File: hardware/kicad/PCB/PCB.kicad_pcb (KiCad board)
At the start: 2 copper layers, 19 parts, among them J1 USB_C_Receptacle_PowerOnly_6P, J2 Conn_01x05_Socket, J3 Conn_01x02, U1 STM32G030F6Px, U2 MCP73831-2-OT, U3 DW01A, U4 FS8205A_C2830320

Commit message: updated PCB design
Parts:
- added C4: 1uF, Capacitor_SMD:C_0603_1608Metric, F.Cu at (18.0, 23.8)
- added C5: 1uF, Capacitor_SMD:C_0603_1608Metric, F.Cu at (18.0, 26.3)
- added C6: 100nF, Capacitor_SMD:C_0603_1608Metric, F.Cu at (18.0, 28.8)
- added D10: LED, Diode_SMD:D_0603_1608Metric, F.Cu at (38.1, 18.9)
- added D11: LED, Diode_SMD:D_0603_1608Metric, F.Cu at (38.1, 21.5)
- added D12: LED, Diode_SMD:D_0603_1608Metric, F.Cu at (38.1, 24.1)
- added D13: LED, Diode_SMD:D_0603_1608Metric, F.Cu at (38.1, 26.7)
- added D14: LED, Diode_SMD:D_0603_1608Metric, F.Cu at (38.1, 29.2)
- added D15: LED, Diode_SMD:D_0603_1608Metric, F.Cu at (38.1, 31.8)
- added D16: LED, Diode_SMD:D_0603_1608Metric, F.Cu at (42.2, 16.3)
- added D17: LED, Diode_SMD:D_0603_1608Metric, F.Cu at (42.2, 18.9)
- added D18: LED, Diode_SMD:D_0603_1608Metric, F.Cu at (42.2, 21.5)
- added D19: LED, Diode_SMD:D_0603_1608Metric, F.Cu at (42.2, 24.1)
- added D20: LED, Diode_SMD:D_0603_1608Metric, F.Cu at (42.2, 26.7)
- added D21: LED, Diode_SMD:D_0603_1608Metric, F.Cu at (42.2, 29.2)
- added D22: LED, Diode_SMD:D_0603_1608Metric, F.Cu at (42.2, 31.8)
- added D3: D_Schottky, Sensor_Humidity:Sensirion_DFN-4_1.5x1.5mm_P0.8mm_SHT4x_NoCentralPad, F.Cu at (46.2, 31.4)
- added D4: LED, Diode_SMD:D_0603_1608Metric, F.Cu at (34.1, 21.5)
- added D5: LED, Diode_SMD:D_0603_1608Metric, F.Cu at (34.1, 24.1)
- added D6: LED, Diode_SMD:D_0603_1608Metric, F.Cu at (34.1, 26.7)
- added D7: LED, Diode_SMD:D_0603_1608Metric, F.Cu at (34.1, 29.2)
- added D8: LED, Diode_SMD:D_0603_1608Metric, F.Cu at (34.1, 31.8)
- added D9: LED, Diode_SMD:D_0603_1608Metric, F.Cu at (38.1, 16.3)
- added R10: 470, Resistor_SMD:R_0603_1608Metric, F.Cu at (22.0, 31.3)
- added R11: 470, Resistor_SMD:R_0603_1608Metric, F.Cu at (22.0, 33.8)
- added R12: 470, Resistor_SMD:R_0603_1608Metric, F.Cu at (22.0, 36.3)
- added R13: 470, Resistor_SMD:R_0603_1608Metric, F.Cu at (26.0, 16.3)
- added R14: 470, Resistor_SMD:R_0603_1608Metric, F.Cu at (26.0, 18.8)
- added R15: 470, Resistor_SMD:R_0603_1608Metric, F.Cu at (26.0, 21.3)
- added R16: 470, Resistor_SMD:R_0603_1608Metric, F.Cu at (26.0, 23.8)
- added R17: 470, Resistor_SMD:R_0603_1608Metric, F.Cu at (26.0, 26.3)
- added R18: 470, Resistor_SMD:R_0603_1608Metric, F.Cu at (26.0, 28.8)
- added R19: 470, Resistor_SMD:R_0603_1608Metric, F.Cu at (26.0, 31.3)
- added R20: 470, Resistor_SMD:R_0603_1608Metric, F.Cu at (26.0, 33.8)
- added R21: 470, Resistor_SMD:R_0603_1608Metric, F.Cu at (26.0, 36.3)
- added R22: 470, Resistor_SMD:R_0603_1608Metric, F.Cu at (30.0, 16.3)
- added R23: 470, Resistor_SMD:R_0603_1608Metric, F.Cu at (30.0, 18.8)
- added R24: 470, Resistor_SMD:R_0603_1608Metric, F.Cu at (30.0, 21.3)
- added R25: 470, Resistor_SMD:R_0603_1608Metric, F.Cu at (30.0, 23.8)
- added R26: 470, Resistor_SMD:R_0603_1608Metric, F.Cu at (30.0, 26.3)
- added R27: 1M, Resistor_SMD:R_0603_1608Metric, F.Cu at (30.0, 28.8)
- added R28: 1M, Resistor_SMD:R_0603_1608Metric, F.Cu at (30.0, 31.3)
- added R7: 470, Resistor_SMD:R_0603_1608Metric, F.Cu at (22.0, 23.8)
- added R8: 470, Resistor_SMD:R_0603_1608Metric, F.Cu at (22.0, 26.3)
- added R9: 470, Resistor_SMD:R_0603_1608Metric, F.Cu at (22.0, 28.8)
- added U5: TPS7A0233PDBVR, JLC2KiCad:SOT-23-5_L2.9-W1.6-P0.95-LS2.8-BR, F.Cu at (46.6, 27.6)
- moved U4 33.3 mm to (46.9, 22.9)
- moved R5 31.3 mm to (22.0, 18.8)
- moved R6 31.3 mm to (22.0, 21.3)
- moved R4 31.3 mm to (22.0, 16.3)
- moved D1 31.3 mm to (34.1, 16.3)
- moved D2 31.3 mm to (34.1, 18.9)
- moved KEY1 23.4 mm to (47.6, 17.7)
- moved C1 19.0 mm to (18.0, 16.3)
- moved C2 19.0 mm to (18.0, 18.8)
- moved C3 19.0 mm to (18.0, 21.3)
- moved J3 18.4 mm to (37.3, 46.7)
- moved J2 16.6 mm to (23.5, 40.0)
- moved R2 13.6 mm to (18.0, 33.8)
- moved R3 13.6 mm to (18.0, 36.3)
- moved R1 13.6 mm to (18.0, 31.3)
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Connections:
- D2 pad 1: unconnected-(D2-K-Pad1) -> TIM14_CH1
- D2 pad 2: unconnected-(D2-A-Pad2) -> Net-(D2-A)
- J2 pad 1: unconnected-(J2-Pin_1-Pad1) -> Net-(D3-A)
- U1 pad 1: unconnected-(U1-PB7/PB8-Pad1) -> TIM16_CH1
- U1 pad 11: unconnected-(U1-PA4-Pad11) -> TIM14_CH1
- U1 pad 13: unconnected-(U1-PA6-Pad13) -> TIM3_CH1
- U1 pad 14: unconnected-(U1-PA7-Pad14) -> TIM3_CH2
- U1 pad 15: unconnected-(U1-PA8/PB0/PB1/PB2-Pad15) -> TIM1_CH2N
- U1 pad 16: unconnected-(U1-PA9/PA11-Pad16) -> TIM1_CH4
- U1 pad 20: unconnected-(U1-PB3/PB4/PB5/PB6-Pad20) -> TIM1_CH3
- U1 pad 4: unconnected-(U1-VDD-Pad4) -> PROG_PWR
- U1 pad 8: unconnected-(U1-PA1-Pad8) -> PA1

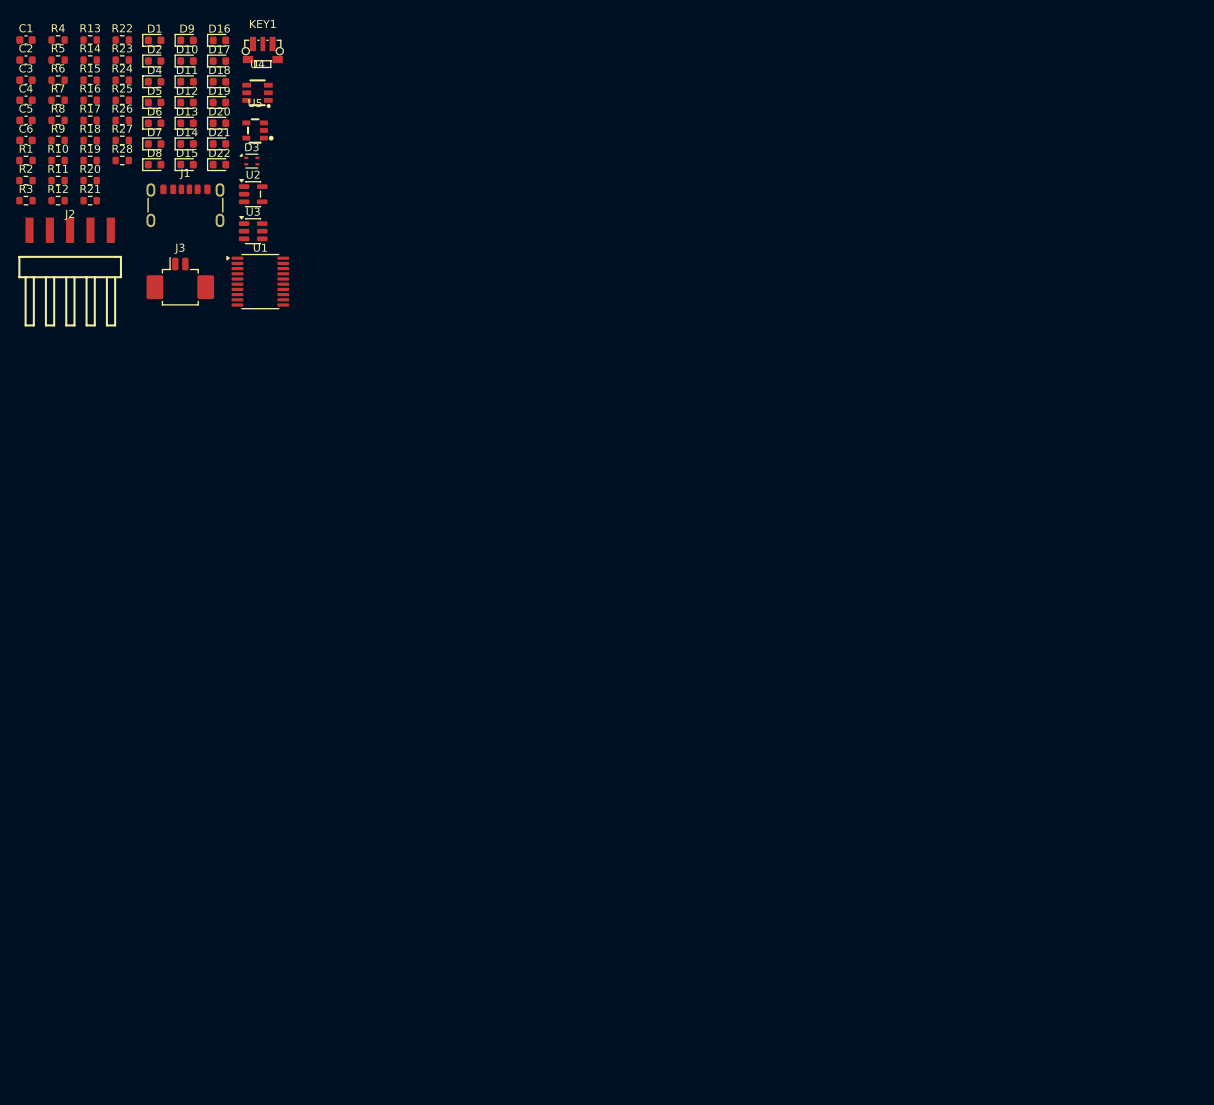
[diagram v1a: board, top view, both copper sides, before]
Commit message: Major update to PCB layout, nearly ready for first batch (#8)
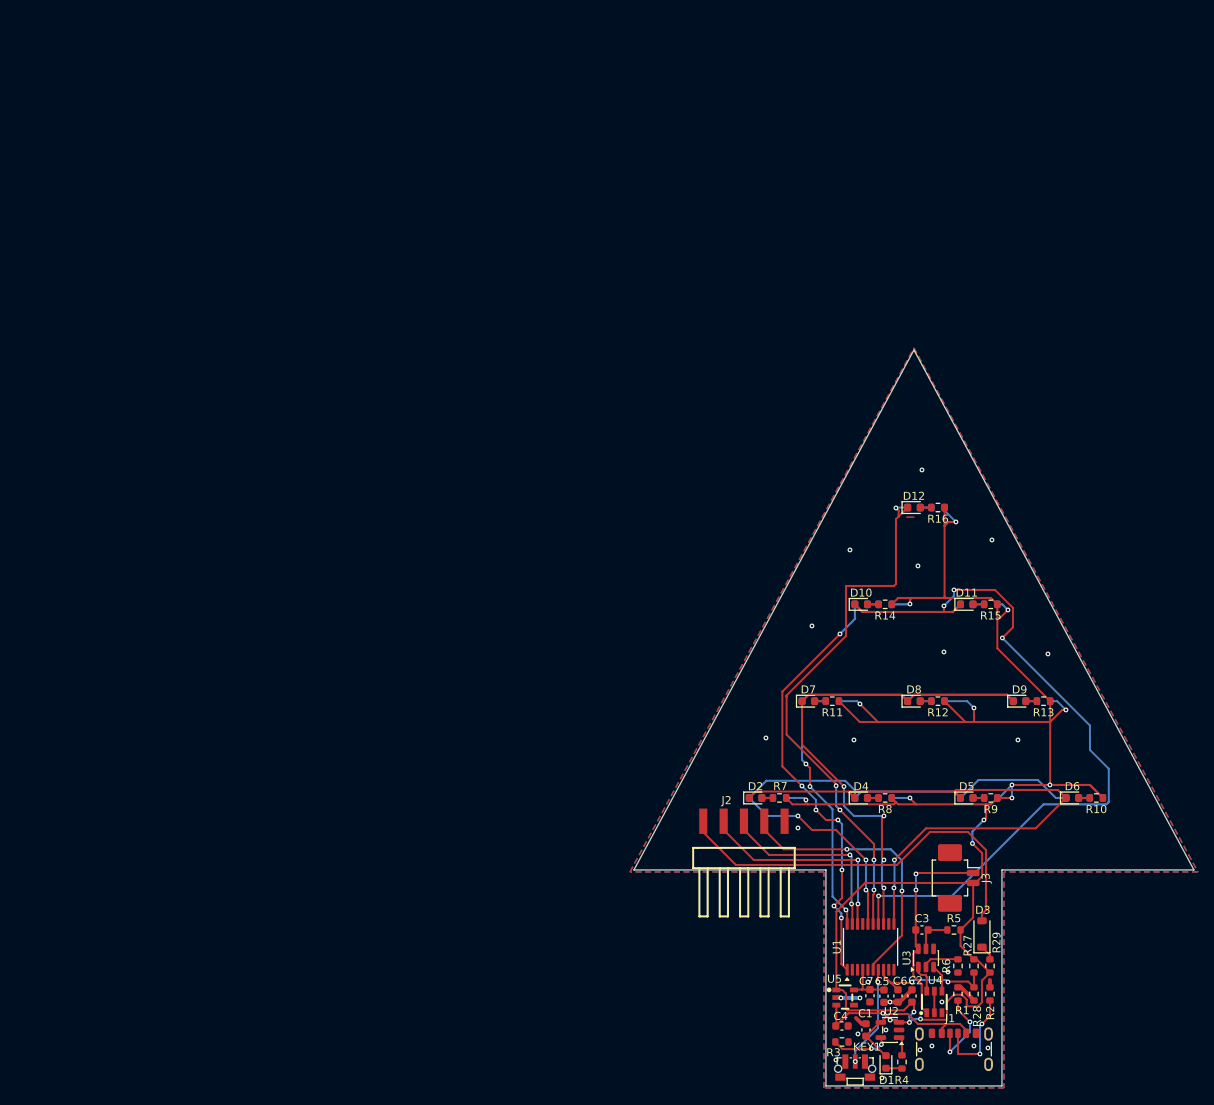
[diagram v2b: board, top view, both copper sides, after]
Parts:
- added C7: 100nF, Capacitor_SMD:C_0603_1608Metric, F.Cu at (123.5, 135.7)
- added R29: 33, Resistor_SMD:R_0603_1608Metric, F.Cu at (138.5, 132.0)
- D13, D14, D15, D16, D17, D18, D19, D20, D21, D22, R17, R18, R19, R20, R21, R22, R23, R24, R25, R26: moved to B.Cu
- D3: footprint Sensor_Humidity:Sensirion_DFN-4_1.5x1.5mm_P0.8mm_SHT4x_NoCentralPad -> Diode_SMD:D_SOD-123
- moved R4 165.7 mm to (127.5, 144.0), turned to 90 degrees
- moved C1 162.3 mm to (123.0, 140.0), turned to -90 degrees
- moved C2 161.1 mm to (128.8, 135.8), turned to 90 degrees
- moved R6 157.8 mm to (134.5, 132.0), turned to 90 degrees
- moved R2 157.7 mm to (138.5, 135.5), turned to 90 degrees
- moved D1 157.1 mm to (125.5, 144.0), turned to 90 degrees
- moved R1 156.3 mm to (134.5, 135.5), turned to 90 degrees
- moved R5 156.1 mm to (134.0, 127.5)
- moved C3 154.4 mm to (130.0, 127.5)
- moved C4 154.2 mm to (120.0, 139.5)
- moved C5 153.3 mm to (125.2, 135.8), turned to 90 degrees
- moved C6 152.7 mm to (127.0, 135.8), turned to -90 degrees
- moved R10 152.3 mm to (151.8, 111.0), turned to 180 degrees
- moved R28 149.0 mm to (136.5, 135.5), turned to -90 degrees
- moved R27 148.3 mm to (136.5, 132.0), turned to -90 degrees
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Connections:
- C5 pad 2: PROG_PWR -> Net-(U1-VDD)
- D3 pad 1: PROG_PWR -> Net-(D3-K)
- U1 pad 4: PROG_PWR -> Net-(U1-VDD)
- U5 pad 5: PROG_PWR -> Net-(U1-VDD)
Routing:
- net V_Bat: track 0.00 -> 267.8 mm, vias 0 -> 18
- net TIM3_CH2: track 0.00 -> 93.0 mm, vias 0 -> 4
- net TIM14_CH1: track 0.00 -> 75.3 mm, vias 0 -> 2
- net TIM1_CH4: track 0.00 -> 70.4 mm, vias 0 -> 3
- net TIM1_CH2N: track 0.00 -> 69.2 mm, vias 0 -> 5
- net TIM16_CH1: track 0.00 -> 68.5 mm, vias 0 -> 7
- net TIM3_CH1: track 0.00 -> 62.4 mm, vias 0 -> 4
- net TIM1_CH3: track 0.00 -> 57.9 mm, vias 0 -> 3
- net Net-(D3-A): track 0.00 -> 50.1 mm
- net NRST: track 0.00 -> 35.0 mm, vias 0 -> 2
- net SWDIO: track 0.00 -> 27.4 mm, vias 0 -> 2
- net Bat_Neg: track 0.00 -> 25.6 mm, vias 0 -> 2
- net SWCLK: track 0.00 -> 24.4 mm, vias 0 -> 2
- net V_USB: track 0.00 -> 19.8 mm
- net PA1: track 0.00 -> 16.0 mm, vias 0 -> 2
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- added copper zone on B.Cu, net GND
- added copper zone on F.Cu, net GND
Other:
- board outline added: 70 x 92 mm

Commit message: First revision of the board ready
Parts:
- added C8: 100nF, Capacitor_SMD:C_0603_1608Metric, F.Cu at (116.3, 115.8)
- C3: value 0.1uF -> 100nF
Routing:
- net NRST: track 35.0 -> 36.7 mm
- net GND: track 11.6 -> 12.6 mm, vias 25 -> 24
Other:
- board text added: "By HenrikBiscuit"
- board text added: "Gran Ornament Rev1"
